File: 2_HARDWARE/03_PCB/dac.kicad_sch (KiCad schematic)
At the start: 12 parts, among them U17 AD9850, U18 AD9744

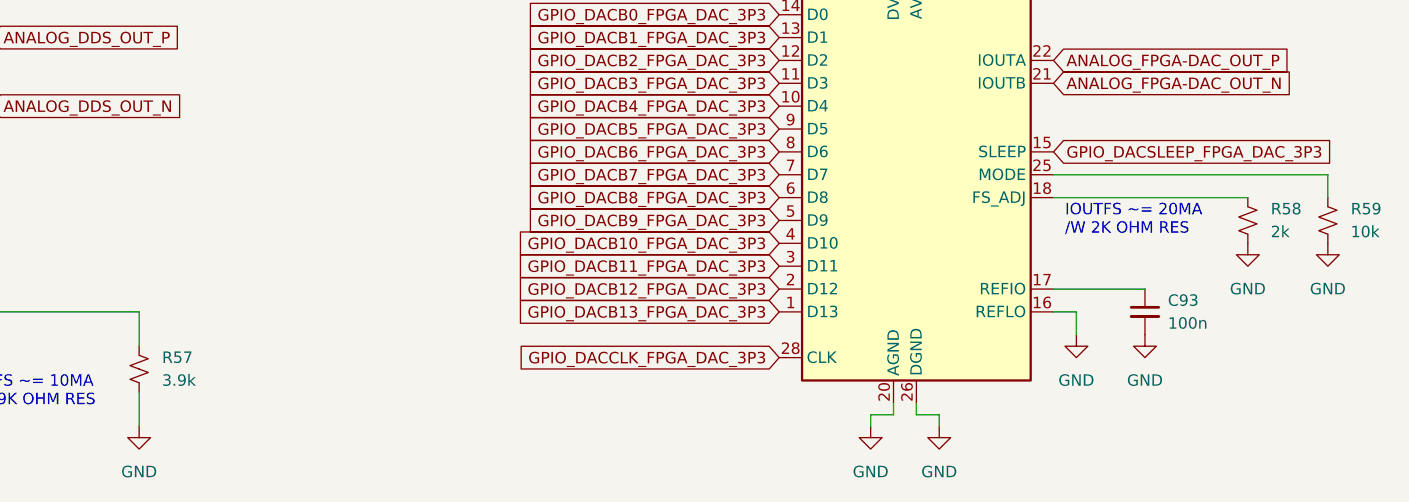
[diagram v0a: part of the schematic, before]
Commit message: MINOR: Changed Boot Select Switches to Pull-Downs / Pull Up DNI and continued layout.
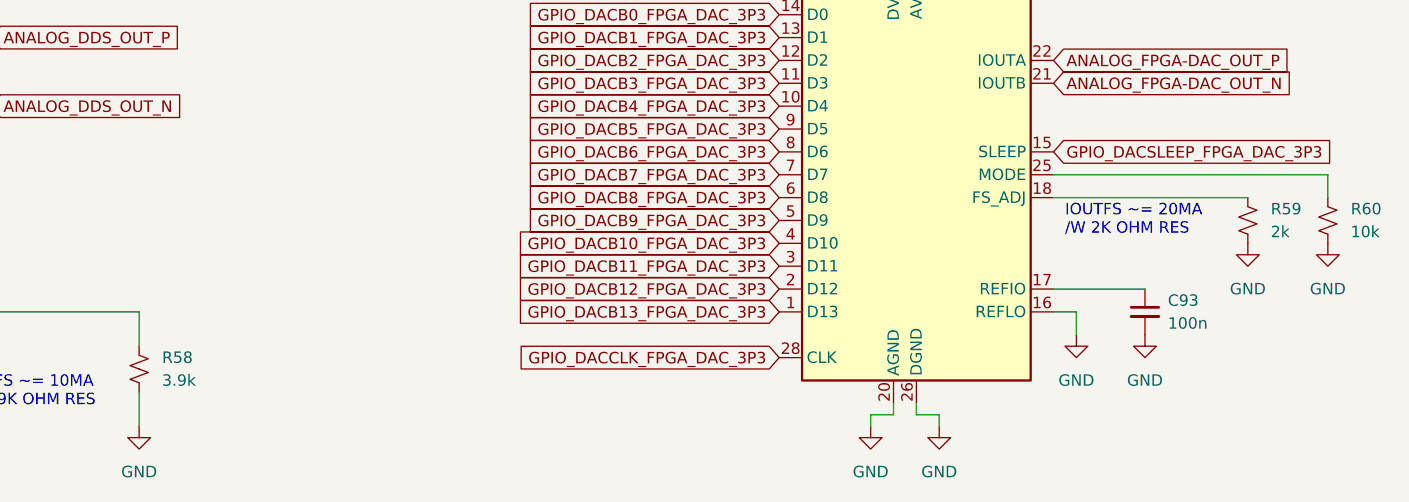
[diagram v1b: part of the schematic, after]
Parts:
- renumbered R57 to R58, R58 to R59, R59 to R60
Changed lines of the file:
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@@
 		(dnp no)
 		(fields_autoplaced yes)
-		(property "Reference" "#PWR0230"
+		(property "Reference" "#PWR0226"
 			(at 204.47 120.65 0)
 			(effects
@@
 			(project "arb"
 				(path "/866ef9be-3b01-4288-a6e0-a2357aa17e50/7126ceca-2dec-4994-855f-f217c0acdc71"
-					(reference "#PWR0230")
+					(reference "#PWR0226")
 					(unit 1)
 				)
@@
 		(dnp no)
 		(fields_autoplaced yes)
-		(property "Reference" "#PWR0236"
+		(property "Reference" "#PWR0232"
 			(at 234.95 110.49 0)
 			(effects
@@
 			(project "arb"
 				(path "/866ef9be-3b01-4288-a6e0-a2357aa17e50/7126ceca-2dec-4994-855f-f217c0acdc71"
-					(reference "#PWR0236")
+					(reference "#PWR0232")
 					(unit 1)
 				)
@@
 		(dnp no)
 		(fields_autoplaced yes)
-		(property "Reference" "#PWR0231"
+		(property "Reference" "#PWR0227"
 			(at 212.09 120.65 0)
 			(effects
@@
 			(project "arb"
 				(path "/866ef9be-3b01-4288-a6e0-a2357aa17e50/7126ceca-2dec-4994-855f-f217c0acdc71"
-					(reference "#PWR0231")
+					(reference "#PWR0227")
 					(unit 1)
 				)
@@
 		(dnp no)
 		(fields_autoplaced yes)
-		(property "Reference" "#PWR0218"
+		(property "Reference" "#PWR0214"
 			(at 93.98 64.77 0)
 			(effects
@@
 			(project "arb"
 				(path "/866ef9be-3b01-4288-a6e0-a2357aa17e50/7126ceca-2dec-4994-855f-f217c0acdc71"
-					(reference "#PWR0218")
+					(reference "#PWR0214")
 					(unit 1)
 				)
@@
 		(dnp no)
 		(fields_autoplaced yes)
-		(property "Reference" "#PWR0227"
+		(property "Reference" "#PWR0223"
 			(at 137.16 46.99 0)
 			(effects
@@
 			(project "arb"
 				(path "/866ef9be-3b01-4288-a6e0-a2357aa17e50/7126ceca-2dec-4994-855f-f217c0acdc71"
-					(reference "#PWR0227")
+					(reference "#PWR0223")
 					(unit 1)
 				)
@@
 		(dnp no)
 		(fields_autoplaced yes)
-		(property "Reference" "#PWR0224"
+		(property "Reference" "#PWR0220"
 			(at 123.19 120.65 0)
 			(effects
@@
 			(project "arb"
 				(path "/866ef9be-3b01-4288-a6e0-a2357aa17e50/7126ceca-2dec-4994-855f-f217c0acdc71"
-					(reference "#PWR0224")
+					(reference "#PWR0220")
 					(unit 1)
 				)
@@
 		(dnp no)
 		(fields_autoplaced yes)
-		(property "Reference" "R57"
+		(property "Reference" "R58"
 			(at 125.73 106.6799 0)
 			(effects
@@
 			(project "arb"
 				(path "/866ef9be-3b01-4288-a6e0-a2357aa17e50/7126ceca-2dec-4994-855f-f217c0acdc71"
-					(reference "R57")
+					(reference "R58")
 					(unit 1)
 				)
@@
 		(dnp no)
 		(fields_autoplaced yes)
-		(property "Reference" "#PWR0223"
+		(property "Reference" "#PWR0219"
 			(at 116.84 54.61 0)
 			(effects
@@
 			(project "arb"
 				(path "/866ef9be-3b01-4288-a6e0-a2357aa17e50/7126ceca-2dec-4994-855f-f217c0acdc71"
-					(reference "#PWR0223")
+					(reference "#PWR0219")
 					(unit 1)
 				)
@@
 		(dnp no)
 		(fields_autoplaced yes)
-		(property "Reference" "R59"
+		(property "Reference" "R60"
 			(at 257.81 90.1699 0)
 			(effects
@@
 			(project "arb"
 				(path "/866ef9be-3b01-4288-a6e0-a2357aa17e50/7126ceca-2dec-4994-855f-f217c0acdc71"
-					(reference "R59")
+					(reference "R60")
 					(unit 1)
 				)
@@
 		(dnp no)
 		(fields_autoplaced yes)
-		(property "Reference" "#PWR0232"
+		(property "Reference" "#PWR0228"
 			(at 213.36 60.96 0)
 			(effects
@@
 			(project "arb"
 				(path "/866ef9be-3b01-4288-a6e0-a2357aa17e50/7126ceca-2dec-4994-855f-f217c0acdc71"
-					(reference "#PWR0232")
+					(reference "#PWR0228")
 					(unit 1)
 				)
@@
 		(dnp no)
 		(fields_autoplaced yes)
-		(property "Reference" "#PWR0219"
+		(property "Reference" "#PWR0215"
 			(at 93.98 120.65 0)
 			(effects
@@
 			(project "arb"
 				(path "/866ef9be-3b01-4288-a6e0-a2357aa17e50/7126ceca-2dec-4994-855f-f217c0acdc71"
-					(reference "#PWR0219")
+					(reference "#PWR0215")
 					(unit 1)
 				)
@@
 		(dnp no)
 		(fields_autoplaced yes)
-		(property "Reference" "#PWR0226"
+		(property "Reference" "#PWR0222"
 			(at 127 54.61 0)
 			(effects
@@
 			(project "arb"
 				(path "/866ef9be-3b01-4288-a6e0-a2357aa17e50/7126ceca-2dec-4994-855f-f217c0acdc71"
-					(reference "#PWR0226")
+					(reference "#PWR0222")
 					(unit 1)
 				)
@@
 		(dnp no)
 		(fields_autoplaced yes)
-		(property "Reference" "#PWR0233"
+		(property "Reference" "#PWR0229"
 			(at 227.33 50.8 0)
 			(effects
@@
 			(project "arb"
 				(path "/866ef9be-3b01-4288-a6e0-a2357aa17e50/7126ceca-2dec-4994-855f-f217c0acdc71"
-					(reference "#PWR0233")
+					(reference "#PWR0229")
 					(unit 1)
 				)
@@
 		(dnp no)
 		(fields_autoplaced yes)
-		(property "Reference" "#PWR0240"
+		(property "Reference" "#PWR0236"
 			(at 255.27 100.33 0)
 			(effects
@@
 			(project "arb"
 				(path "/866ef9be-3b01-4288-a6e0-a2357aa17e50/7126ceca-2dec-4994-855f-f217c0acdc71"
-					(reference "#PWR0240")
+					(reference "#PWR0236")
 					(unit 1)
 				)
@@
 		(dnp no)
 		(fields_autoplaced yes)
-		(property "Reference" "R58"
+		(property "Reference" "R59"
 			(at 248.92 90.1699 0)
 			(effects
@@
 			(project "arb"
 				(path "/866ef9be-3b01-4288-a6e0-a2357aa17e50/7126ceca-2dec-4994-855f-f217c0acdc71"
-					(reference "R58")
+					(reference "R59")
 					(unit 1)
 				)
@@
 		(dnp no)
 		(fields_autoplaced yes)
-		(property "Reference" "#PWR0221"
+		(property "Reference" "#PWR0217"
 			(at 106.68 54.61 0)
 			(effects
@@
 			(project "arb"
 				(path "/866ef9be-3b01-4288-a6e0-a2357aa17e50/7126ceca-2dec-4994-855f-f217c0acdc71"
-					(reference "#PWR0221")
+					(reference "#PWR0217")
 					(unit 1)
 				)
@@
 		(dnp no)
 		(fields_autoplaced yes)
-		(property "Reference" "#PWR0216"
+		(property "Reference" "#PWR0212"
 			(at 88.9 69.85 0)
 			(effects
@@
 			(project "arb"
 				(path "/866ef9be-3b01-4288-a6e0-a2357aa17e50/7126ceca-2dec-4994-855f-f217c0acdc71"
-					(reference "#PWR0216")
+					(reference "#PWR0212")
 					(unit 1)
 				)
@@
 		(dnp no)
 		(fields_autoplaced yes)
-		(property "Reference" "#PWR0238"
+		(property "Reference" "#PWR0234"
 			(at 237.49 58.42 0)
 			(effects
@@
 			(project "arb"
 				(path "/866ef9be-3b01-4288-a6e0-a2357aa17e50/7126ceca-2dec-4994-855f-f217c0acdc71"
-					(reference "#PWR0238")
+					(reference "#PWR0234")
 					(unit 1)
 				)
@@
 		(dnp no)
 		(fields_autoplaced yes)
-		(property "Reference" "#PWR0220"
+		(property "Reference" "#PWR0216"
 			(at 106.68 46.99 0)
 			(effects
@@
 			(project "arb"
 				(path "/866ef9be-3b01-4288-a6e0-a2357aa17e50/7126ceca-2dec-4994-855f-f217c0acdc71"
-					(reference "#PWR0220")
+					(reference "#PWR0216")
 					(unit 1)
 				)
@@
 		(dnp no)
 		(fields_autoplaced yes)
-		(property "Reference" "#PWR0234"
+		(property "Reference" "#PWR0230"
 			(at 227.33 58.42 0)
 			(effects
@@
 			(project "arb"
 				(path "/866ef9be-3b01-4288-a6e0-a2357aa17e50/7126ceca-2dec-4994-855f-f217c0acdc71"
-					(reference "#PWR0234")
+					(reference "#PWR0230")
 					(unit 1)
 				)
@@
 		(dnp no)
 		(fields_autoplaced yes)
-		(property "Reference" "#PWR0222"
+		(property "Reference" "#PWR0218"
 			(at 116.84 46.99 0)
 			(effects
@@
 			(project "arb"
 				(path "/866ef9be-3b01-4288-a6e0-a2357aa17e50/7126ceca-2dec-4994-855f-f217c0acdc71"
-					(reference "#PWR0222")
+					(reference "#PWR0218")
 					(unit 1)
 				)
@@
 		(dnp no)
 		(fields_autoplaced yes)
-		(property "Reference" "#PWR0229"
+		(property "Reference" "#PWR0225"
 			(at 203.2 60.96 0)
 			(effects
@@
 			(project "arb"
 				(path "/866ef9be-3b01-4288-a6e0-a2357aa17e50/7126ceca-2dec-4994-855f-f217c0acdc71"
-					(reference "#PWR0229")
+					(reference "#PWR0225")
 					(unit 1)
 				)
@@
 		(dnp no)
 		(fields_autoplaced yes)
-		(property "Reference" "#PWR0239"
+		(property "Reference" "#PWR0235"
 			(at 246.38 100.33 0)
 			(effects
@@
 			(project "arb"
 				(path "/866ef9be-3b01-4288-a6e0-a2357aa17e50/7126ceca-2dec-4994-855f-f217c0acdc71"
-					(reference "#PWR0239")
+					(reference "#PWR0235")
 					(unit 1)
 				)
@@
 		(dnp no)
 		(fields_autoplaced yes)
-		(property "Reference" "#PWR0237"
+		(property "Reference" "#PWR0233"
 			(at 237.49 50.8 0)
 			(effects
@@
 			(project "arb"
 				(path "/866ef9be-3b01-4288-a6e0-a2357aa17e50/7126ceca-2dec-4994-855f-f217c0acdc71"
-					(reference "#PWR0237")
+					(reference "#PWR0233")
 					(unit 1)
 				)
@@
 		(dnp no)
 		(fields_autoplaced yes)
-		(property "Reference" "#PWR0225"
+		(property "Reference" "#PWR0221"
 			(at 127 46.99 0)
 			(effects
@@
 			(project "arb"
 				(path "/866ef9be-3b01-4288-a6e0-a2357aa17e50/7126ceca-2dec-4994-855f-f217c0acdc71"
-					(reference "#PWR0225")
+					(reference "#PWR0221")
 					(unit 1)
 				)
@@
 		(dnp no)
 		(fields_autoplaced yes)
-		(property "Reference" "#PWR0228"
+		(property "Reference" "#PWR0224"
 			(at 137.16 54.61 0)
 			(effects
@@
 			(project "arb"
 				(path "/866ef9be-3b01-4288-a6e0-a2357aa17e50/7126ceca-2dec-4994-855f-f217c0acdc71"
-					(reference "#PWR0228")
+					(reference "#PWR0224")
 					(unit 1)
 				)
@@
 		(dnp no)
 		(fields_autoplaced yes)
-		(property "Reference" "#PWR0217"
+		(property "Reference" "#PWR0213"
 			(at 88.9 115.57 0)
 			(effects
@@
 			(project "arb"
 				(path "/866ef9be-3b01-4288-a6e0-a2357aa17e50/7126ceca-2dec-4994-855f-f217c0acdc71"
-					(reference "#PWR0217")
+					(reference "#PWR0213")
 					(unit 1)
 				)
@@
 		(dnp no)
 		(fields_autoplaced yes)
-		(property "Reference" "#PWR0235"
+		(property "Reference" "#PWR0231"
 			(at 227.33 110.49 0)
 			(effects
@@
 			(project "arb"
 				(path "/866ef9be-3b01-4288-a6e0-a2357aa17e50/7126ceca-2dec-4994-855f-f217c0acdc71"
-					(reference "#PWR0235")
-					(unit 1)
-				)
+					(reference "#PWR0231")
+					(unit 1)
+				)
